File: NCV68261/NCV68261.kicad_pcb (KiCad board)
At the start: 2 copper layers, 8 parts, among them Q1 SiR186LDP, Q2 SiR186LDP, U1 NCV68261

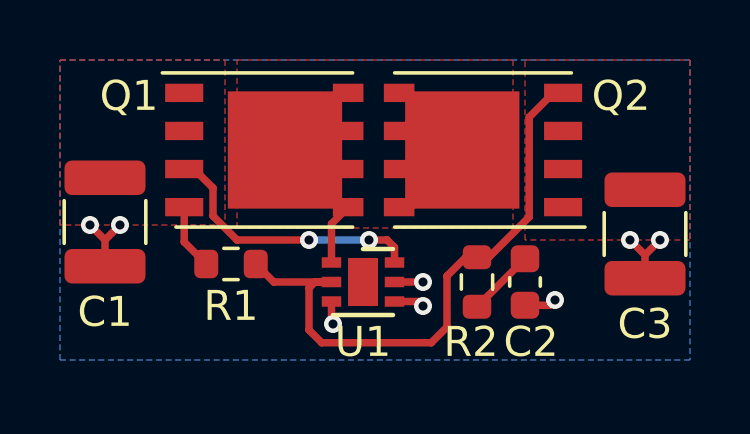
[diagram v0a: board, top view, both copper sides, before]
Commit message: use smaller fets
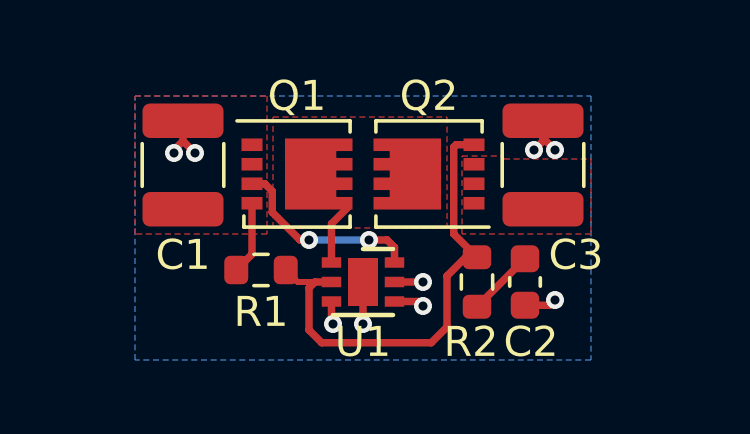
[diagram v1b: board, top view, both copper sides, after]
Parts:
- Q1, Q2: value SiR186LDP -> DMT6007LFG-7; footprint Package_SO:PowerPAK_SO-8_Single -> Package_SON:Diodes_PowerDI3333-8
- moved C3 4.10 mm to (146.6, 80.5), turned to 90 degrees
- moved C1 3.22 mm to (134.6, 80.5), turned to 90 degrees
- moved Q2 1.97 mm to (142.8, 80.8)
- moved Q1 1.35 mm to (138.4, 80.8)
- moved R1 1.02 mm to (137.2, 84.0)
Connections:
- U1 pad 7: (no net) -> GND
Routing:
- net Net-(Q2-Pad4): track 20.0 -> 16.6 mm
- net /V_{BUS}: track 9.14 -> 6.54 mm
- net GND: track 7.27 -> 8.20 mm, vias 7 -> 8
